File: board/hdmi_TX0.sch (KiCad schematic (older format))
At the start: 21 parts

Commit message: Update from templates.
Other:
- note added: "This sheet is generated from ../external/templates/\nDO NOT MODIFY!!!\n8ac8b78"
- note removed: "This sheet is generated from ../external/templates/\nDO NOT MODIFY!!!\n4b96504"
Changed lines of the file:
@@
 	6500 7050 6500 7150
 Text Notes 670  10960 0    197  ~ 39
-This sheet is generated from ../external/templates/\nDO NOT MODIFY!!!\n4b96504
+This sheet is generated from ../external/templates/\nDO NOT MODIFY!!!\n8ac8b78
 Wire Wire Line
 	2255 6970 2325 6970

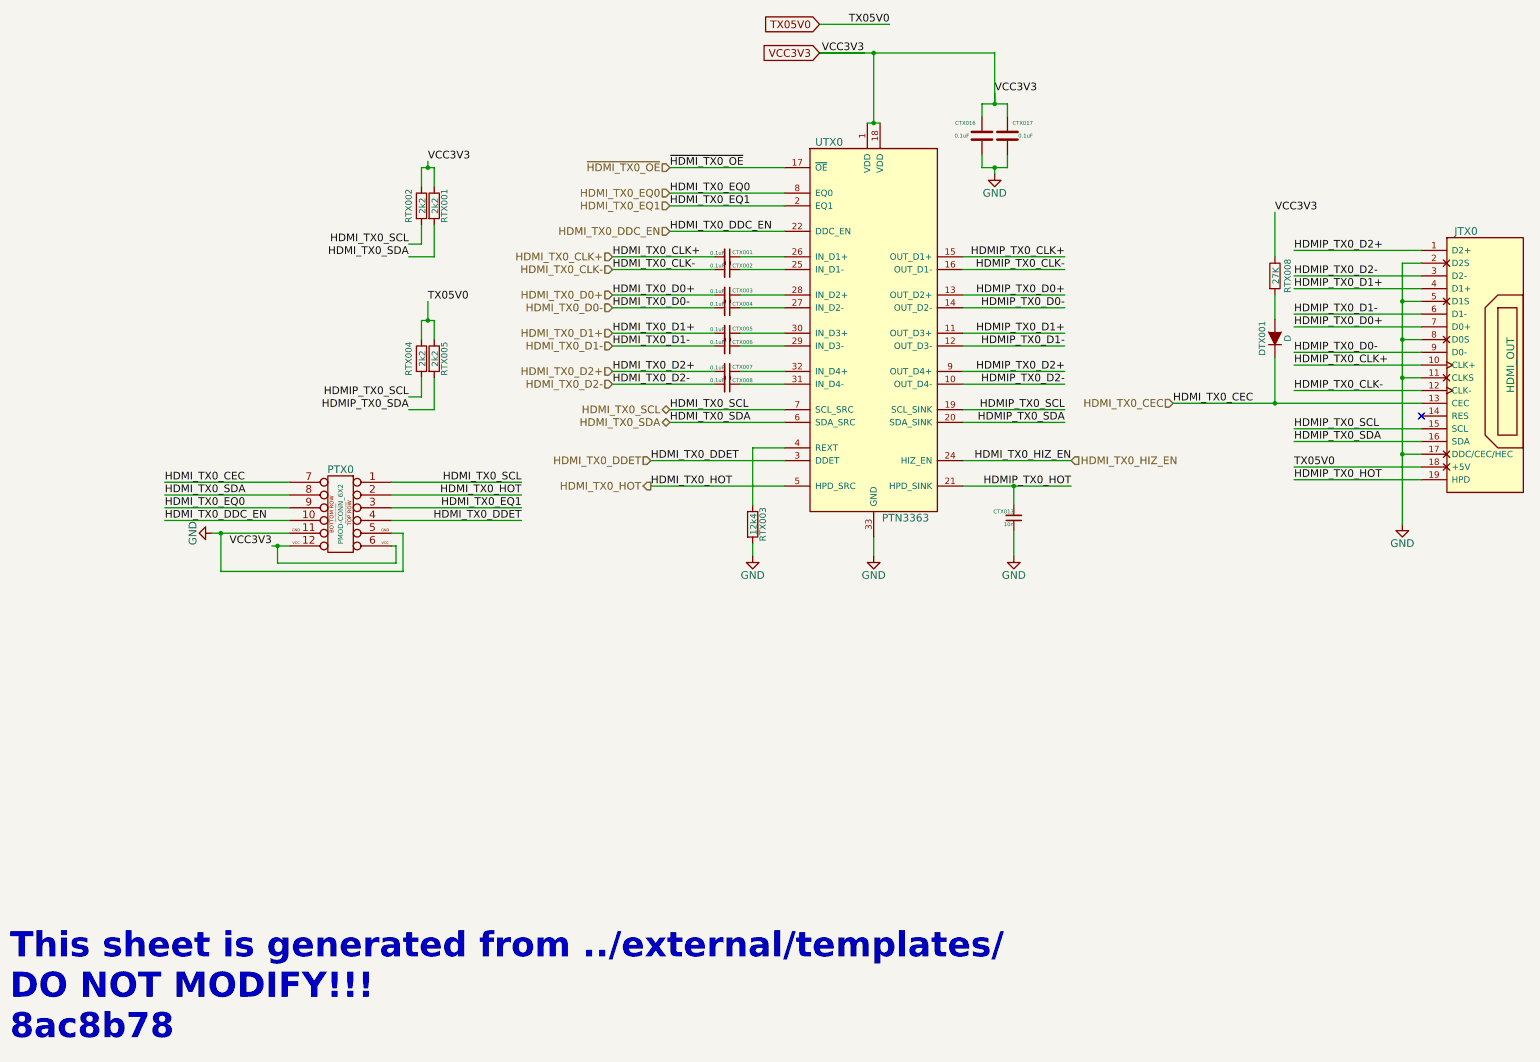
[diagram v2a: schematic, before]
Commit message: Reorganising the high speed signals.
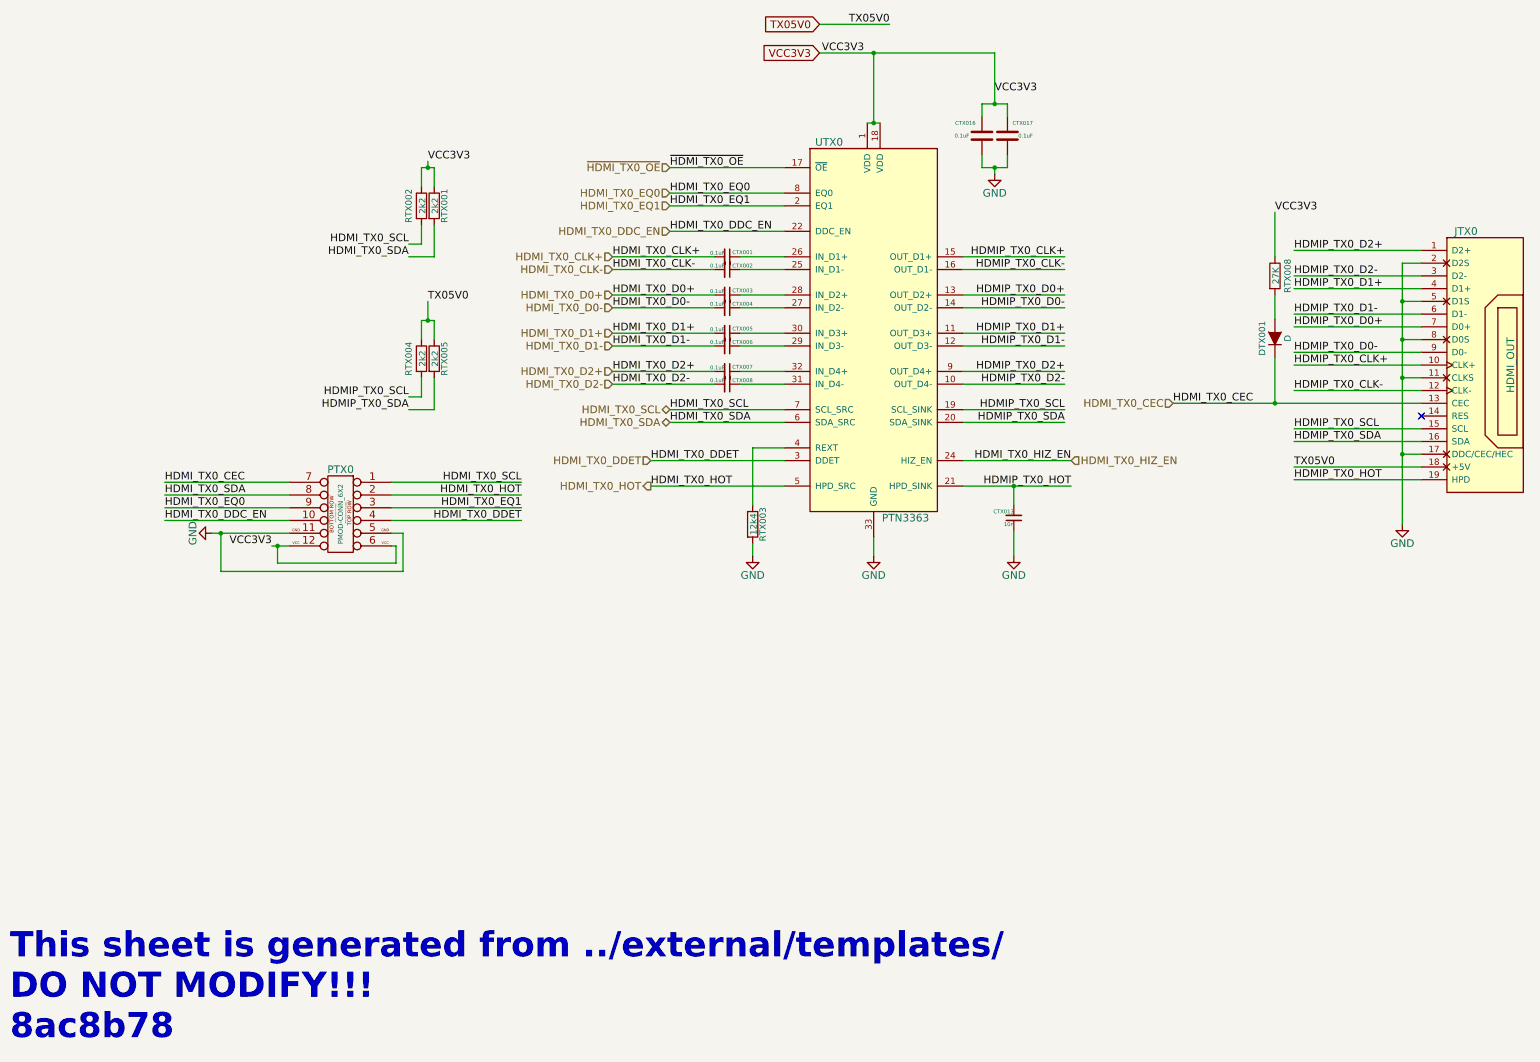
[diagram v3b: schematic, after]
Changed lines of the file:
@@
 HDMIP_TX0_HOT
 $Comp
-L GND #PWR106
+L GND #PWR010
 U 1 1 57B7C214
 P 7450 7150
-F 0 "#PWR106" H 7450 6900 60  0001 C CNN
+F 0 "#PWR010" H 7450 6900 60  0001 C CNN
 F 1 "GND" H 7450 7000 60  0000 C CNN
 F 2 "" H 7450 7150 60  0000 C CNN
@@
 $EndComp
 $Comp
-L GND #PWR112
+L GND #PWR011
 U 1 1 57C0774B
 P 11600 6900
-F 0 "#PWR112" H 11600 6650 60  0001 C CNN
+F 0 "#PWR011" H 11600 6650 60  0001 C CNN
 F 1 "GND" H 11600 6750 60  0000 C CNN
 F 2 "" H 11600 6900 60  0000 C CNN
@@
 AR Path="/57C07751" Ref="RTX008"  Part="1"
 AR Path="/57C01383/57C07751" Ref="RTX003"  Part="1"
+AR Path="/5802F547/57C07751" Ref="RTX008"  Part="1"
 F 0 "RTX008" V 10700 4950 50  0000 C CNN
 F 1 "27K" V 10607 4951 50  0000 C CNN
@@
 AR Path="/57C07753" Ref="RTX002"  Part="1"
 AR Path="/57C01383/57C07753" Ref="RTX001"  Part="1"
+AR Path="/5802F547/57C07753" Ref="RTX002"  Part="1"
 F 0 "RTX002" V 3800 4400 50  0000 C CNN
 F 1 "2k2" V 3907 4401 50  0000 C CNN
@@
 AR Path="/57C07755" Ref="RTX001"  Part="1"
 AR Path="/57C01383/57C07755" Ref="RTX002"  Part="1"
+AR Path="/5802F547/57C07755" Ref="RTX001"  Part="1"
 F 0 "RTX001" V 4080 4400 50  0000 C CNN
 F 1 "2k2" V 4007 4401 50  0000 C CNN
@@
 	11750 4850 11600 4850
 Wire Wire Line
-	11600 4850 11600 5150
-Wire Wire Line
-	11600 5150 11600 5450
-Wire Wire Line
-	11600 5450 11600 5750
-Wire Wire Line
-	11600 5750 11600 6350
-Wire Wire Line
-	11600 6350 11600 6900
+	11600 4850 11600 6900
 Wire Wire Line
 	11750 5150 11600 5150
@@
 	6400 5800 6750 5800
 Wire Wire Line
-	8150 6600 8550 6600
-Wire Wire Line
-	8550 6600 9000 6600
+	8150 6600 9000 6600
 Wire Wire Line
 	8150 6400 9000 6400
 Wire Wire Line
-	7400 3750 7450 3750
-Wire Wire Line
-	7450 3750 7500 3750
-Wire Wire Line
-	7450 3750 7450 3200
+	7400 3750 7500 3750
+Wire Wire Line
+	7450 3200 7450 3750
 Connection ~ 7450 3750
 Wire Wire Line
@@
 Connection ~ 11600 6350
 Wire Wire Line
-	9800 5950 10600 5950
-Wire Wire Line
-	10600 5950 11750 5950
+	9800 5950 11750 5950
 Wire Wire Line
 	10600 5950 10600 5590
@@
 	4000 4100 4000 4250
 Wire Wire Line
-	3900 4100 3950 4100
-Wire Wire Line
-	3950 4100 4000 4100
+	3900 4100 4000 4100
 Text Label 3800 5900 2    60   ~ 0
 HDMIP_TX0_SCL
@@
 AR Path="/57C07769" Ref="RTX004"  Part="1"
 AR Path="/57C01383/57C07769" Ref="RTX004"  Part="1"
+AR Path="/5802F547/57C07769" Ref="RTX004"  Part="1"
 F 0 "RTX004" V 3800 5600 50  0000 C CNN
 F 1 "2k2" V 3907 5601 50  0000 C CNN
@@
 AR Path="/57B7FCE7" Ref="RTX005"  Part="1"
 AR Path="/57C01383/57B7FCE7" Ref="RTX005"  Part="1"
+AR Path="/5802F547/57B7FCE7" Ref="RTX005"  Part="1"
 F 0 "RTX005" V 4080 5600 50  0000 C CNN
 F 1 "2k2" V 4007 5601 50  0000 C CNN
@@
 AR Path="/57C0776D" Ref="RTX003"  Part="1"
 AR Path="/57C01383/57C0776D" Ref="RTX006"  Part="1"
+AR Path="/5802F547/57C0776D" Ref="RTX003"  Part="1"
 F 0 "RTX003" V 6580 6900 50  0000 C CNN
 F 1 "12k4" V 6507 6901 50  0000 C CNN
@@
 	6500 6300 6500 6750
 $Comp
-L GND #PWR104
+L GND #PWR012
 U 1 1 57C0776F
 P 6500 7150
-F 0 "#PWR104" H 6500 6900 60  0001 C CNN
+F 0 "#PWR012" H 6500 6900 60  0001 C CNN
 F 1 "GND" H 6500 7000 60  0000 C CNN
 F 2 "" H 6500 7150 60  0000 C CNN
@@
 	3900 5300 3900 5450
 Wire Wire Line
-	3900 5300 3950 5300
-Wire Wire Line
-	3950 5300 4000 5300
+	3900 5300 4000 5300
 Wire Wire Line
 	4000 5300 4000 5450
@@
 $EndComp
 $Comp
-L GND #PWR109
+L GND #PWR013
 U 1 1 57C07776
 P 8550 7150
-F 0 "#PWR109" H 8550 6900 60  0001 C CNN
+F 0 "#PWR013" H 8550 6900 60  0001 C CNN
 F 1 "GND" H 8550 7000 60  0000 C CNN
 F 2 "" H 8550 7150 60  0000 C CNN
@@
 AR Path="/57C07777" Ref="CTX017"  Part="1"
 AR Path="/57C01383/57C07777" Ref="CTX002"  Part="1"
+AR Path="/5802F547/57C07777" Ref="CTX017"  Part="1"
 F 0 "CTX017" H 8300 3750 30  0000 L CNN
 F 1 "0.1uF" H 8300 3850 30  0000 L CNN
@@
 AR Path="/57C07779" Ref="CTX016"  Part="1"
 AR Path="/57C01383/57C07779" Ref="CTX001"  Part="1"
+AR Path="/5802F547/57C07779" Ref="CTX016"  Part="1"
 F 0 "CTX016" H 8350 3750 30  0000 L CNN
 F 1 "0.1uF" H 8400 3850 30  0000 L CNN
@@
 $EndComp
 Wire Wire Line
-	8300 3600 8400 3600
-Wire Wire Line
-	8400 3600 8500 3600
+	8300 3600 8500 3600
 Wire Wire Line
 	8300 3600 8300 3700
@@
 	8300 4000 8300 4100
 Wire Wire Line
-	8300 4100 8400 4100
-Wire Wire Line
-	8400 4100 8500 4100
+	8300 4100 8500 4100
 Wire Wire Line
 	8500 4100 8500 4000
 $Comp
-L GND #PWR108
+L GND #PWR014
 U 1 1 57C0777E
 P 8400 4150
-F 0 "#PWR108" H 8400 3900 60  0001 C CNN
+F 0 "#PWR014" H 8400 3900 60  0001 C CNN
 F 1 "GND" H 8400 4000 60  0000 C CNN
 F 2 "" H 8400 4150 60  0000 C CNN
@@
 HDMI_TX0_SDA
 $Comp
-L GND #PWR101
+L GND #PWR015
 U 1 1 57C07784
 P 2255 6970
-F 0 "#PWR101" H 2255 6720 60  0001 C CNN
+F 0 "#PWR015" H 2255 6720 60  0001 C CNN
 F 1 "GND" H 2255 6820 60  0000 C CNN
 F 2 "" H 2255 6970 60  0000 C CNN
@@
 This sheet is generated from ../external/templates/\nDO NOT MODIFY!!!\n8ac8b78
 Wire Wire Line
-	2255 6970 2325 6970
-Wire Wire Line
-	2325 6970 2865 6970
-Wire Wire Line
-	2725 7070 2770 7070
-Wire Wire Line
-	2770 7070 2865 7070
+	2255 6970 2865 6970
+Wire Wire Line
+	2725 7070 2865 7070
 Wire Wire Line
 	2865 6570 1885 6570
@@
 VCC3V3
 Wire Wire Line
-	7025 3200 7375 3200
+	7025 3200 8400 3200
 $Comp
 L PMOD-CONN_6X2 PTX0
@@
 $EndComp
 Wire Wire Line
-	8400 3600 8400 3515
+	8400 3200 8400 3600
 Text Label 8400 3515 0    60   ~ 0
 VCC3V3
@@
 Text GLabel 7025 2975 0    60   Input ~ 0
 TX05V0
-Wire Wire Line
-	7025 3200 7450 3200
-Wire Wire Line
-	7450 3200 8400 3200
-Wire Wire Line
-	8400 3200 8400 3600
 Connection ~ 7450 3200
 Wire Wire Line

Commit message: Working on making the high speed lines better.
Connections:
- net HDMIA_TX0_CLK+: now reaches CTX001.1, UTX0.26 (IN_D1+)
- net HDMIA_TX0_CLK-: now reaches CTX002.1, UTX0.25 (IN_D1-)
- net HDMIA_TX0_D0-: now reaches CTX004.1, UTX0.27 (IN_D2-)
- net HDMIA_TX0_D0+: now reaches CTX003.1, UTX0.28 (IN_D2+)
- net HDMIA_TX0_D1-: now reaches CTX006.1, UTX0.29 (IN_D3-)
- net HDMIA_TX0_D1+: now reaches CTX005.1, UTX0.30 (IN_D3+)
- net HDMIA_TX0_D2-: now reaches CTX008.1, UTX0.31 (IN_D4-)
- net HDMIA_TX0_D2+: now reaches CTX007.1, UTX0.32 (IN_D4+)
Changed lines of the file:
@@
 $Descr A3 16535 11693
 encoding utf-8
-Sheet 1 2
+Sheet 2 2
 Title ""
 Date ""
@@
 Wire Wire Line
 	7025 2975 7575 2975
+Text Label 6550 4800 0    20   ~ 0
+HDMIA_TX0_CLK+
+Text Label 6550 4900 0    20   ~ 0
+HDMIA_TX0_CLK-
+Text Label 6550 5100 0    20   ~ 0
+HDMIA_TX0_D0+
+Text Label 6550 5200 0    20   ~ 0
+HDMIA_TX0_D0-
+Text Label 6550 5400 0    20   ~ 0
+HDMIA_TX0_D1+
+Text Label 6550 5500 0    20   ~ 0
+HDMIA_TX0_D1-
+Text Label 6550 5700 0    20   ~ 0
+HDMIA_TX0_D2+
+Text Label 6550 5800 0    20   ~ 0
+HDMIA_TX0_D2-
 $EndSCHEMATC
